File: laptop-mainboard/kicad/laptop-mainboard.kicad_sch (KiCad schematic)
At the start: 0 parts

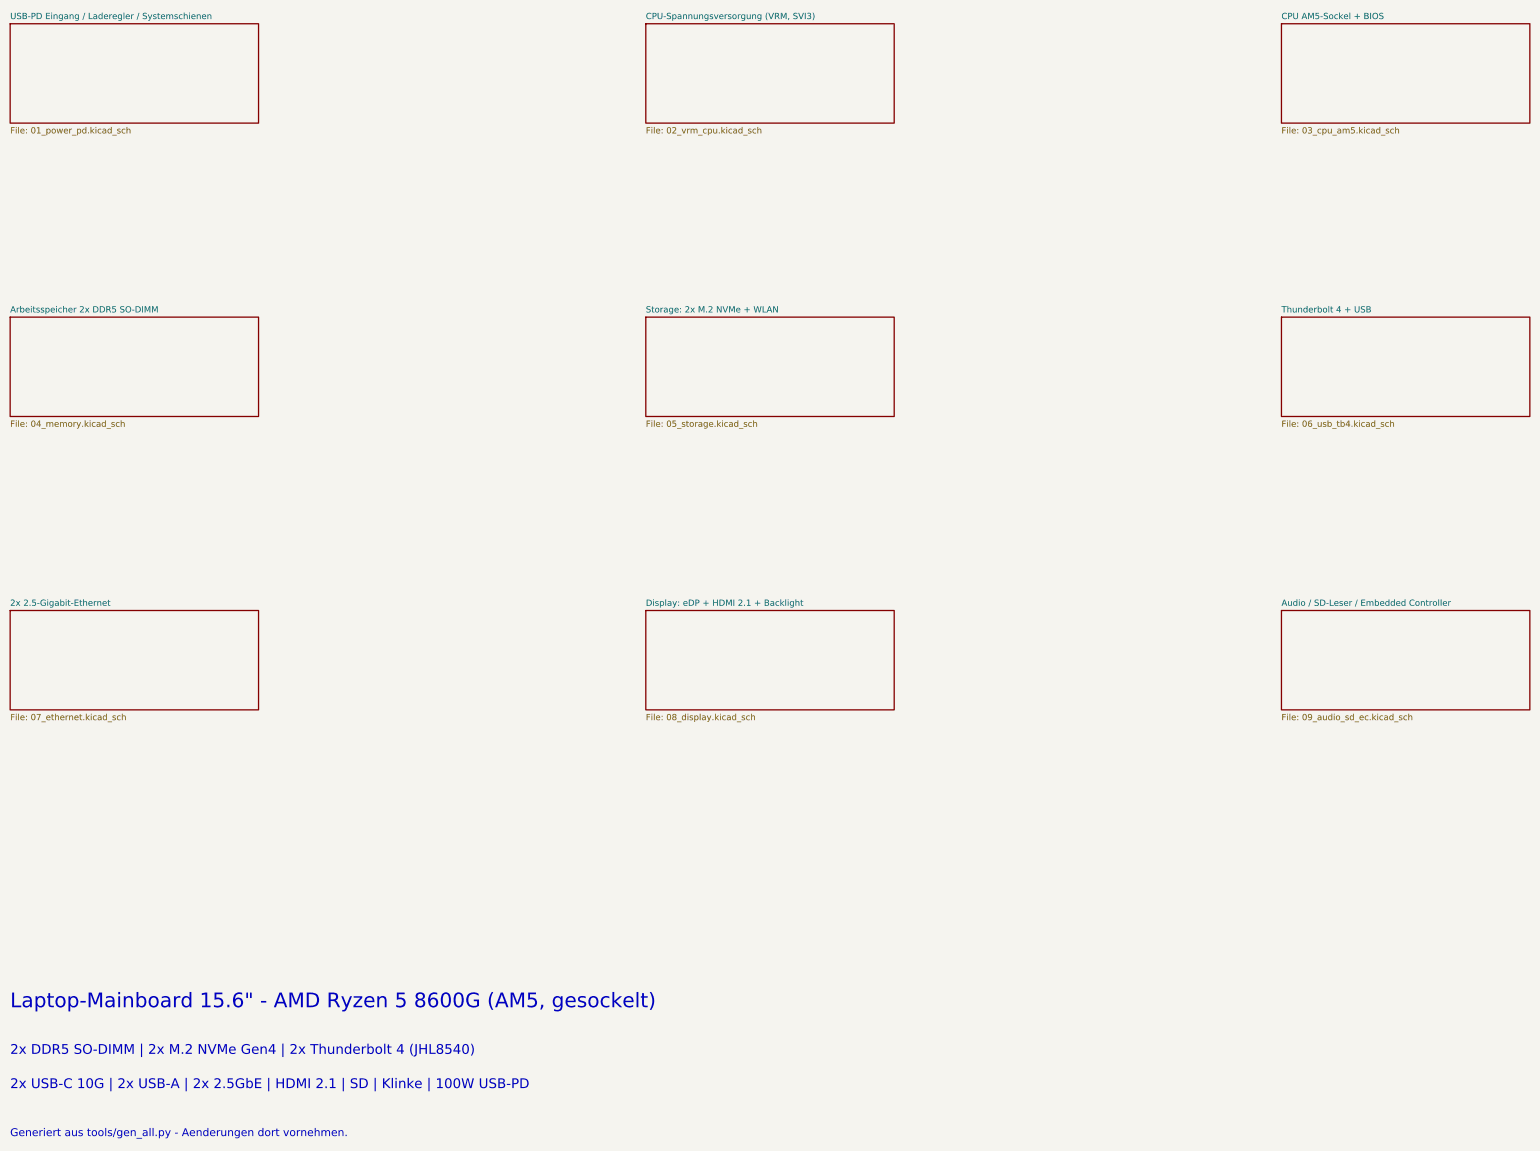
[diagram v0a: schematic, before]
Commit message: Rev B: echte AM5-Pinbelegung, Kleinteile, EliteBook-850-G7-Format
- AM5-Pinmap (1718 Pins, WikiChip/Wikimedia Public Domain) als CSV,
  Sockel-Footprint mit echten Padnamen und 1708 Signal-Netzen im Board
- Blatt 10: MLCC-Baenke, 11 ESD-Arrays, USB2-Chokes, Straps; 48-MHz-Quarz;
  beidseitige Bestueckung (B.Cu) mit Kollisionspruefung pro Seite
- Board 340x112mm im EliteBook-850-G7-Layout: USB-C-100W-PD an der
  Barrel-Jack-Position, TB4/HDMI/USB-A/RJ45 rechts, USB-A/Klinke links,
  HP-Akku 3S/56Wh, HP-FPC-Steckplaetze (Pinouts zu verifizieren)
- GND-Stitching-Vias, MDI-/DP-Korridore, 645 Board-Netze
- Renderer tools/render_board.py erzeugt docs/board_render.png
- Doku: elitebook.md neu, grenzen.md/README/power/layout aktualisiert

Co-Authored-By: Claude Fable 5 <noreply@anthropic.com>
Claude-Session: https://claude.ai/code/session_01E8mU1RUAv938Hs69waADCc
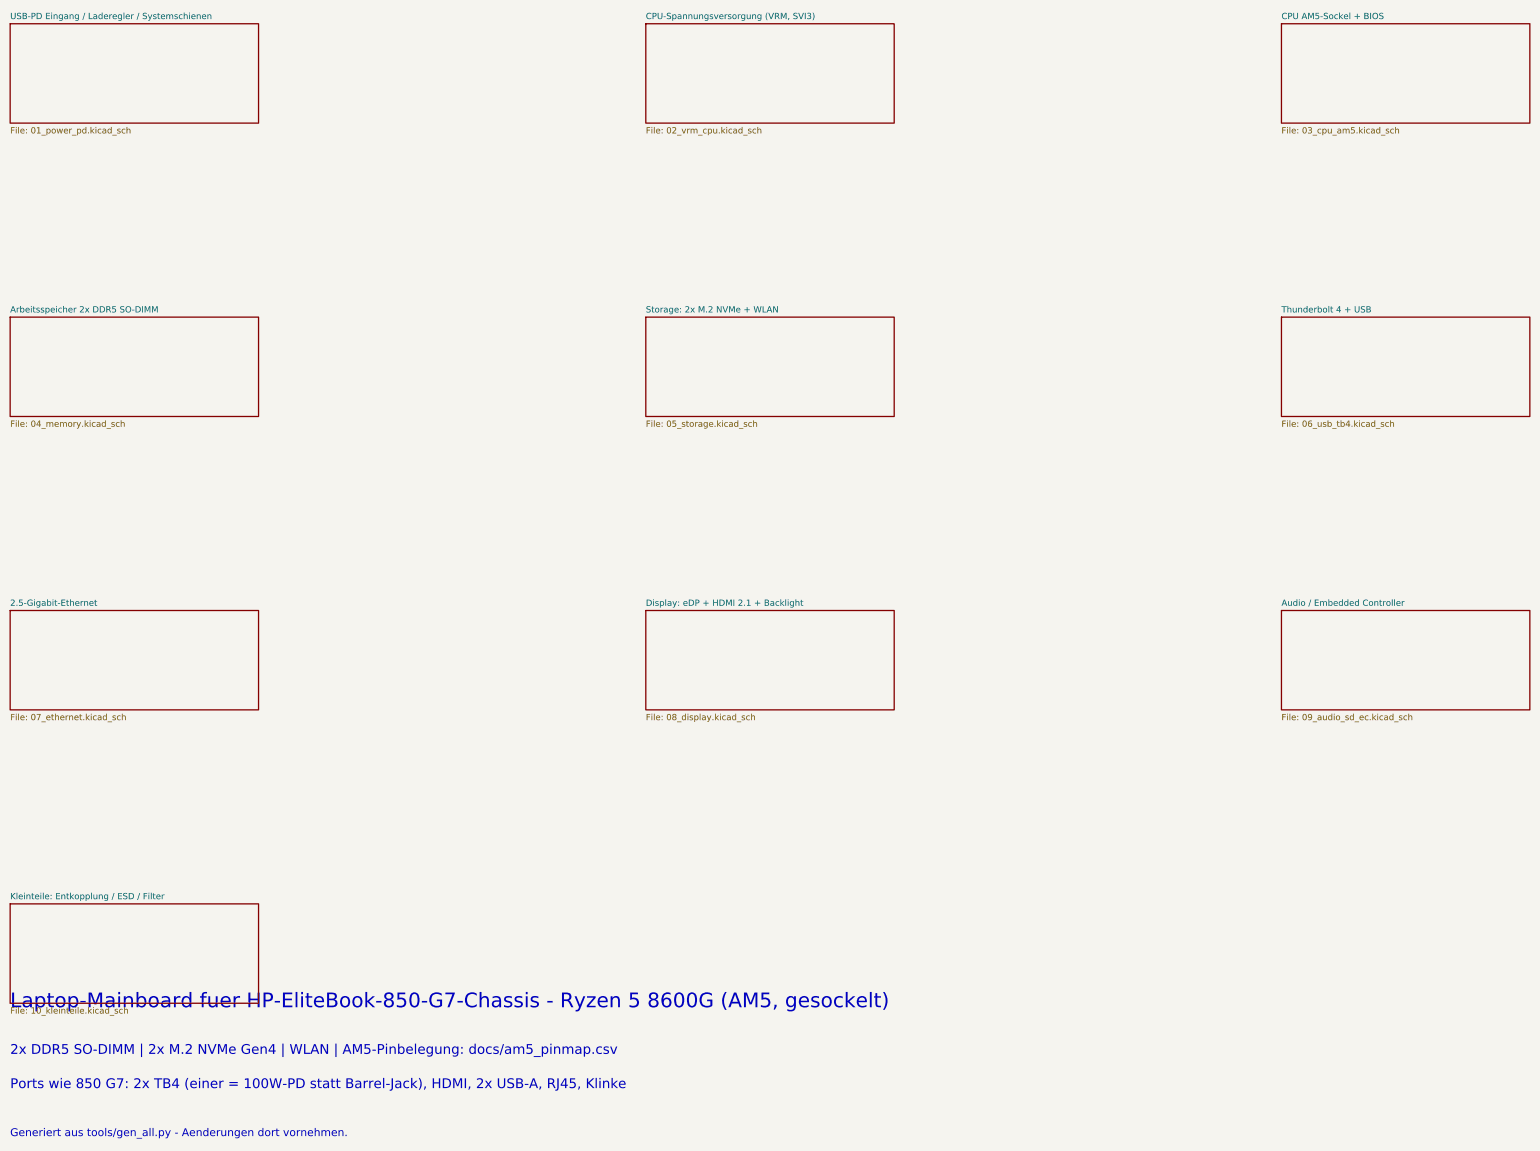
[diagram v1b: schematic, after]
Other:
- removed sheet 2x 2.5-Gigabit-Ethernet
- removed sheet Audio / SD-Leser / Embedded Controller
- added sheet 2.5-Gigabit-Ethernet (07_ethernet.kicad_sch)
- added sheet Audio / Embedded Controller (09_audio_sd_ec.kicad_sch)
- added sheet Kleinteile: Entkopplung / ESD / Filter (10_kleinteile.kicad_sch)
- note added: "2x DDR5 SO-DIMM | 2x M.2 NVMe Gen4 | WLAN | AM5-Pinbelegung: docs/am5_pinmap.csv"
- note added: "Laptop-Mainboard fuer HP-EliteBook-850-G7-Chassis - Ryzen 5 8600G (AM5, gesockelt)"
- note added: "Ports wie 850 G7: 2x TB4 (einer = 100W-PD statt Barrel-Jack), HDMI, 2x USB-A, RJ45, Klinke"
- note removed: "2x DDR5 SO-DIMM | 2x M.2 NVMe Gen4 | 2x Thunderbolt 4 (JHL8540)"
- note removed: "2x USB-C 10G | 2x USB-A | 2x 2.5GbE | HDMI 2.1 | SD | Klinke | 100W USB-PD"
- note removed: "Laptop-Mainboard 15.6" - AMD Ryzen 5 8600G (AM5, gesockelt)"
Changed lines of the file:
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@@
     (company "Laptop-Mainboard-Projekt")
   )
-  (text "Laptop-Mainboard 15.6\" - AMD Ryzen 5 8600G (AM5, gesockelt)" (exclude_from_sim no) (at 30 240 0)
+  (text "Laptop-Mainboard fuer HP-EliteBook-850-G7-Chassis - Ryzen 5 8600G (AM5, gesockelt)" (exclude_from_sim no) (at 30 240 0)
     (effects (font (size 3 3)) (justify left))
   )
-  (text "2x DDR5 SO-DIMM | 2x M.2 NVMe Gen4 | 2x Thunderbolt 4 (JHL8540)" (exclude_from_sim no) (at 30 250 0)
+  (text "2x DDR5 SO-DIMM | 2x M.2 NVMe Gen4 | WLAN | AM5-Pinbelegung: docs/am5_pinmap.csv" (exclude_from_sim no) (at 30 250 0)
     (effects (font (size 2 2)) (justify left))
   )
-  (text "2x USB-C 10G | 2x USB-A | 2x 2.5GbE | HDMI 2.1 | SD | Klinke | 100W USB-PD" (exclude_from_sim no) (at 30 257 0)
+  (text "Ports wie 850 G7: 2x TB4 (einer = 100W-PD statt Barrel-Jack), HDMI, 2x USB-A, RJ45, Klinke" (exclude_from_sim no) (at 30 257 0)
     (effects (font (size 2 2)) (justify left))
   )
@@
     (stroke (width 0.1524) (type solid))
     (fill (color 0 0 0 0.0000))
-    (property "Sheetname" "2x 2.5-Gigabit-Ethernet" (at 30 159.2 0)
+    (property "Sheetname" "2.5-Gigabit-Ethernet" (at 30 159.2 0)
       (effects (font (size 1.27 1.27)) (justify left bottom))
     )
@@
     (stroke (width 0.1524) (type solid))
     (fill (color 0 0 0 0.0000))
-    (property "Sheetname" "Audio / SD-Leser / Embedded Controller" (at 290 159.2 0)
+    (property "Sheetname" "Audio / Embedded Controller" (at 290 159.2 0)
       (effects (font (size 1.27 1.27)) (justify left bottom))
     )
@@
     (instances (project "laptop-mainboard" (path "/d22f2c28-8e23-5b8e-ba77-63ae2c13187c" (page "10"))))
   )
+  (sheet (at 30 220) (size 50.8 20.32) (fields_autoplaced yes)
+    (stroke (width 0.1524) (type solid))
+    (fill (color 0 0 0 0.0000))
+    (property "Sheetname" "Kleinteile: Entkopplung / ESD / Filter" (at 30 219.2 0)
+      (effects (font (size 1.27 1.27)) (justify left bottom))
+    )
+    (property "Sheetfile" "10_kleinteile.kicad_sch" (at 30 241.1 0)
+      (effects (font (size 1.27 1.27)) (justify left top))
+    )
+    (instances (project "laptop-mainboard" (path "/d22f2c28-8e23-5b8e-ba77-63ae2c13187c" (page "11"))))
+  )
   (sheet_instances (path "/" (page "1")))

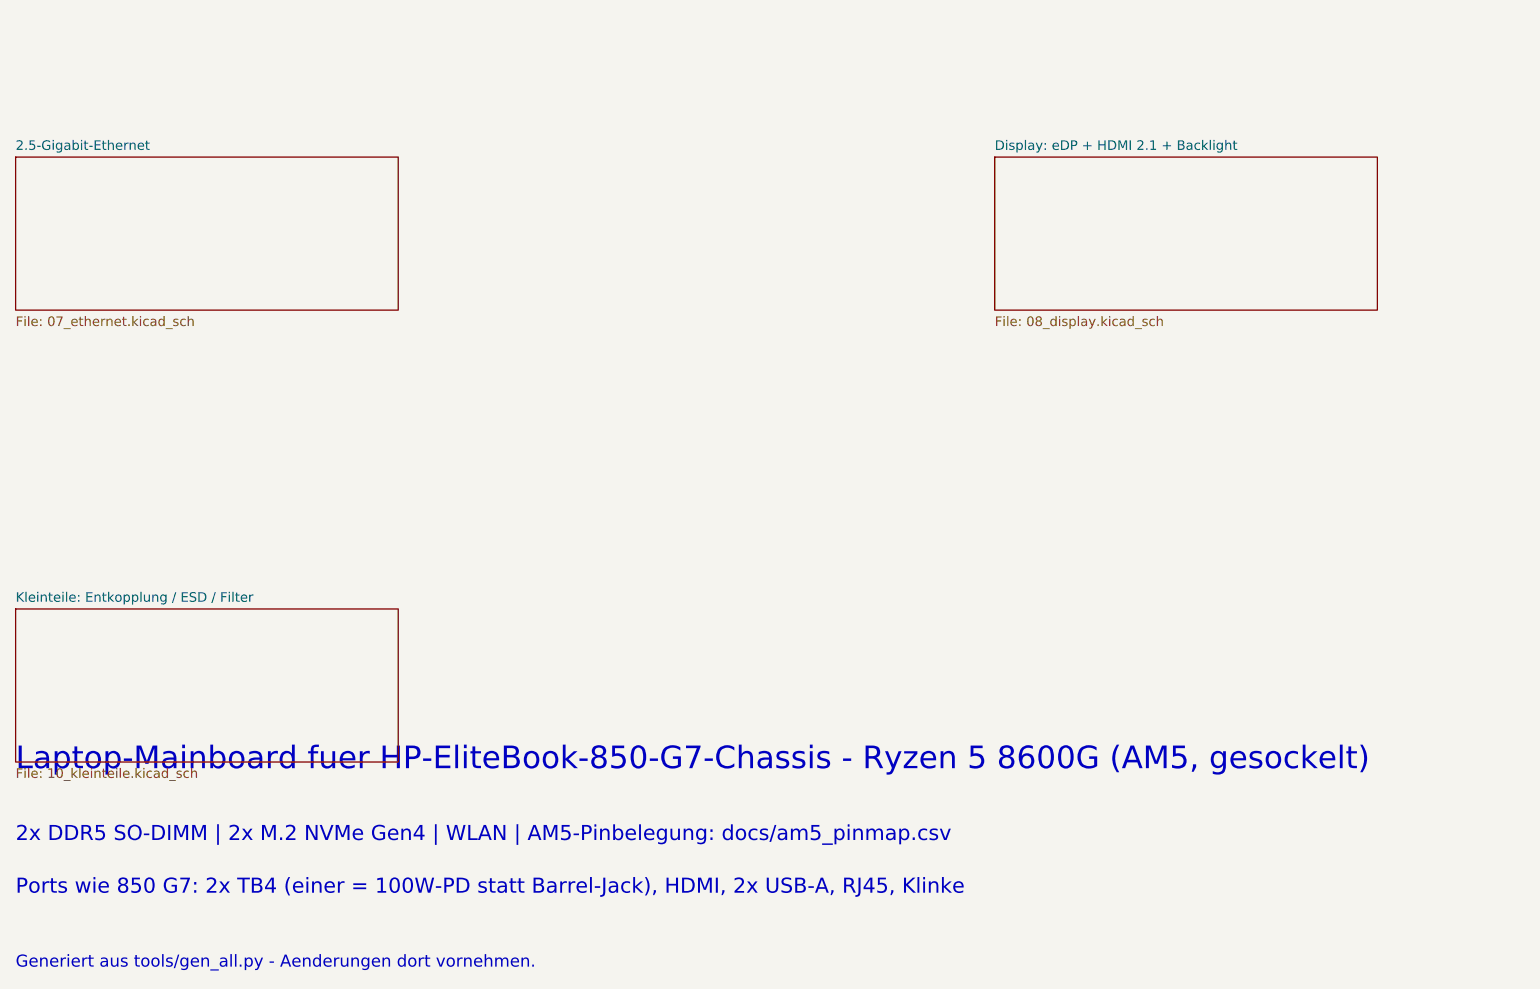
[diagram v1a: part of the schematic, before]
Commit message: Portlayout nach Fotos des Originalgeraets korrigiert
- Rechte Kante hinten->vorn: USB-C-Ladeport 100W (Barrel-Position,
  eigener TPS65987D + Config-Flash, neues Blatt 07_ladeport), USB-A,
  HDMI, 2x USB-C Thunderbolt 4 nebeneinander (JHL8540)
- Kein RJ45 (Original hat keines): Ethernet entfernt, G0/G1 Reserve
- TPS65988 nur noch Source fuer die TB-Ports; breite VBUS_IN-Trasse
  vom Ladeport zum BQ25731
- Interne Anschlusspositionen des Original-Mainboards (Nutzerfoto)
  als Referenztabelle in docs/elitebook.md dokumentiert
- Doku, Blockdiagramm, BOM und Rendering aktualisiert

Co-Authored-By: Claude Fable 5 <noreply@anthropic.com>
Claude-Session: https://claude.ai/code/session_01E8mU1RUAv938Hs69waADCc
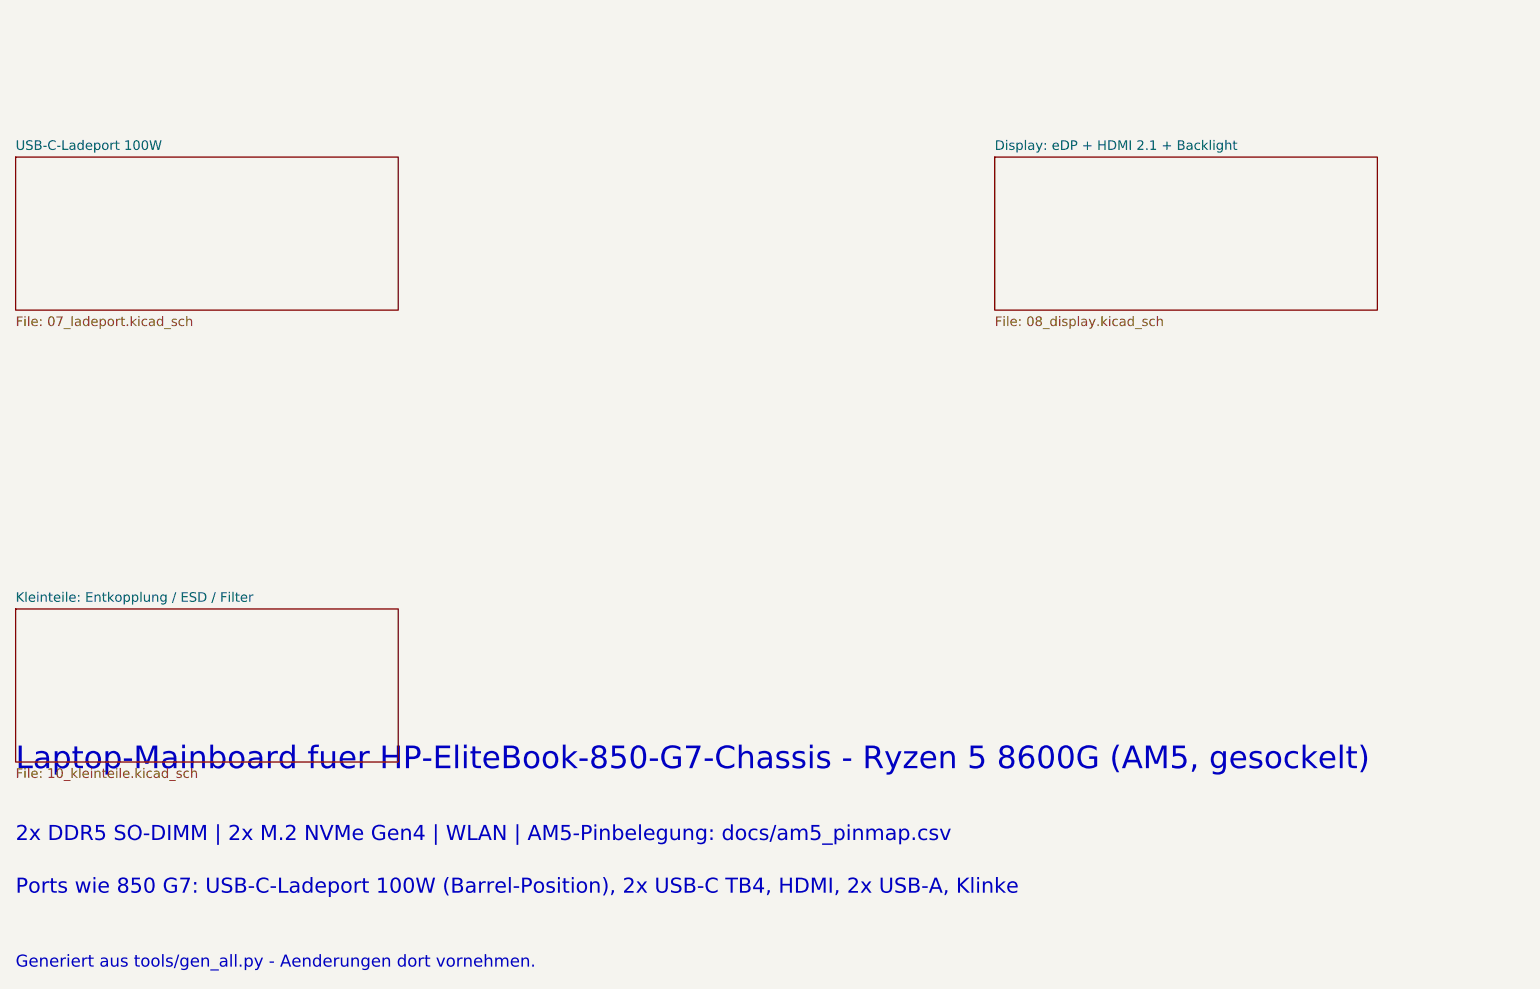
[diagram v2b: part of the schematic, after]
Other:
- removed sheet 2.5-Gigabit-Ethernet
- added sheet USB-C-Ladeport 100W (07_ladeport.kicad_sch)
- note added: "Ports wie 850 G7: USB-C-Ladeport 100W (Barrel-Position), 2x USB-C TB4, HDMI, 2x USB-A, Klinke"
- note removed: "Ports wie 850 G7: 2x TB4 (einer = 100W-PD statt Barrel-Jack), HDMI, 2x USB-A, RJ45, Klinke"
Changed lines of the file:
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@@
     (effects (font (size 2 2)) (justify left))
   )
-  (text "Ports wie 850 G7: 2x TB4 (einer = 100W-PD statt Barrel-Jack), HDMI, 2x USB-A, RJ45, Klinke" (exclude_from_sim no) (at 30 257 0)
+  (text "Ports wie 850 G7: USB-C-Ladeport 100W (Barrel-Position), 2x USB-C TB4, HDMI, 2x USB-A, Klinke" (exclude_from_sim no) (at 30 257 0)
     (effects (font (size 2 2)) (justify left))
   )
@@
     (stroke (width 0.1524) (type solid))
     (fill (color 0 0 0 0.0000))
-    (property "Sheetname" "2.5-Gigabit-Ethernet" (at 30 159.2 0)
+    (property "Sheetname" "USB-C-Ladeport 100W" (at 30 159.2 0)
       (effects (font (size 1.27 1.27)) (justify left bottom))
     )
-    (property "Sheetfile" "07_ethernet.kicad_sch" (at 30 181.1 0)
+    (property "Sheetfile" "07_ladeport.kicad_sch" (at 30 181.1 0)
       (effects (font (size 1.27 1.27)) (justify left top))
     )
